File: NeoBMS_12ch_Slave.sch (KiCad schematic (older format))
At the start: 69 parts, among them IC1 LTC6804-2, P1 Low Cells, P2 High Cells, P3 BUS, P4 Expansion, Q1 Q_NPN_BCEC, SW1 Address, T1 CM Choke, T2 PE-68386N

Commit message: - integrated balancer and filter resistors into one - changed filter/balancer resistors to 1206 - changed BIAS network to 1k5 + 470R - relocated BIAS network
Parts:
- removed R10, R11, R12, R13, R2, R3, R4, R5, R6, R7, R8, R9: 100, Resistors_SMD:R_0805, symbol R
- R28, R29, R30, R31, R32, R33, R34, R35, R36, R37, R38, R39: footprint Resistors_SMD:R_0805 -> Resistors_SMD:R_1206
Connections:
- net Cell_1+: now also IC1.25 (S1)
- net Cell_10+: now also IC1.7 (S10)
- net Cell_11+: now also IC1.5 (S11)
- net Cell_12+: now also IC1.3 (S12)
- net Cell_2+: now also IC1.23 (S2)
- net Cell_3+: now also IC1.21 (S3)
- net Cell_4+: now also IC1.19 (S4)
- net Cell_5+: now also IC1.17 (S5)
- net Cell_6+: now also IC1.15 (S6)
- net Cell_7+: now also IC1.13 (S7)
- net Cell_8+: now also IC1.11 (S8)
- net Cell_9+: now also IC1.9 (S9)
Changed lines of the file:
@@
-$EndComp
-$Comp
-L R R2
-U 1 1 565ED732
-P 3250 2750
-F 0 "R2" V 3330 2750 50  0000 C CNN
-F 1 "100" V 3250 2750 50  0000 C CNN
-F 2 "Resistors_SMD:R_0805" V 3180 2750 30  0001 C CNN
-F 3 "" H 3250 2750 30  0000 C CNN
-	1    3250 2750
-	0    -1   -1   0
-$EndComp
-$Comp
-L R R3
-U 1 1 565ED81C
-P 3250 2950
-F 0 "R3" V 3330 2950 50  0000 C CNN
-F 1 "100" V 3250 2950 50  0000 C CNN
-F 2 "Resistors_SMD:R_0805" V 3180 2950 30  0001 C CNN
-F 3 "" H 3250 2950 30  0000 C CNN
-	1    3250 2950
-	0    -1   -1   0
-$EndComp
-$Comp
-L R R4
-U 1 1 565ED83F
-P 3250 3150
-F 0 "R4" V 3330 3150 50  0000 C CNN
-F 1 "100" V 3250 3150 50  0000 C CNN
-F 2 "Resistors_SMD:R_0805" V 3180 3150 30  0001 C CNN
-F 3 "" H 3250 3150 30  0000 C CNN
-	1    3250 3150
-	0    -1   -1   0
-$EndComp
-$Comp
-L R R5
-U 1 1 565ED85F
-P 3250 3350
-F 0 "R5" V 3330 3350 50  0000 C CNN
-F 1 "100" V 3250 3350 50  0000 C CNN
-F 2 "Resistors_SMD:R_0805" V 3180 3350 30  0001 C CNN
-F 3 "" H 3250 3350 30  0000 C CNN
-	1    3250 3350
-	0    -1   -1   0
-$EndComp
-$Comp
-L R R6
-U 1 1 565ED90E
-P 3250 3550
-F 0 "R6" V 3330 3550 50  0000 C CNN
-F 1 "100" V 3250 3550 50  0000 C CNN
-F 2 "Resistors_SMD:R_0805" V 3180 3550 30  0001 C CNN
-F 3 "" H 3250 3550 30  0000 C CNN
-	1    3250 3550
-	0    -1   -1   0
-$EndComp
-$Comp
-L R R7
-U 1 1 565ED934
-P 3250 3750
-F 0 "R7" V 3330 3750 50  0000 C CNN
-F 1 "100" V 3250 3750 50  0000 C CNN
-F 2 "Resistors_SMD:R_0805" V 3180 3750 30  0001 C CNN
-F 3 "" H 3250 3750 30  0000 C CNN
-	1    3250 3750
-	0    -1   -1   0
-$EndComp
-$Comp
-L R R8
-U 1 1 565ED95D
-P 3250 3950
-F 0 "R8" V 3330 3950 50  0000 C CNN
-F 1 "100" V 3250 3950 50  0000 C CNN
-F 2 "Resistors_SMD:R_0805" V 3180 3950 30  0001 C CNN
-F 3 "" H 3250 3950 30  0000 C CNN
-	1    3250 3950
-	0    -1   -1   0
-$EndComp
-$Comp
-L R R9
-U 1 1 565EDA21
-P 3250 4150
-F 0 "R9" V 3330 4150 50  0000 C CNN
-F 1 "100" V 3250 4150 50  0000 C CNN
-F 2 "Resistors_SMD:R_0805" V 3180 4150 30  0001 C CNN
-F 3 "" H 3250 4150 30  0000 C CNN
-	1    3250 4150
-	0    -1   -1   0
-$EndComp
-$Comp
-L R R10
-U 1 1 565EDA54
-P 3250 4350
-F 0 "R10" V 3330 4350 50  0000 C CNN
-F 1 "100" V 3250 4350 50  0000 C CNN
-F 2 "Resistors_SMD:R_0805" V 3180 4350 30  0001 C CNN
-F 3 "" H 3250 4350 30  0000 C CNN
-	1    3250 4350
-	0    -1   -1   0
-$EndComp
-$Comp
-L R R11
-U 1 1 565EDA86
-P 3250 4550
-F 0 "R11" V 3330 4550 50  0000 C CNN
-F 1 "100" V 3250 4550 50  0000 C CNN
-F 2 "Resistors_SMD:R_0805" V 3180 4550 30  0001 C CNN
-F 3 "" H 3250 4550 30  0000 C CNN
-	1    3250 4550
-	0    -1   -1   0
-$EndComp
-$Comp
-L R R12
-U 1 1 565EDABB
-P 3250 4750
-F 0 "R12" V 3330 4750 50  0000 C CNN
-F 1 "100" V 3250 4750 50  0000 C CNN
-F 2 "Resistors_SMD:R_0805" V 3180 4750 30  0001 C CNN
-F 3 "" H 3250 4750 30  0000 C CNN
-	1    3250 4750
-	0    -1   -1   0
-$EndComp
-$Comp
-L R R13
-U 1 1 565EDAF3
-P 5650 4850
-F 0 "R13" V 5730 4850 50  0000 C CNN
-F 1 "100" V 5650 4850 50  0000 C CNN
-F 2 "Resistors_SMD:R_0805" V 5580 4850 30  0001 C CNN
-F 3 "" H 5650 4850 30  0000 C CNN
-	1    5650 4850
-	0    -1   -1   0
 $EndComp
 $Comp
@@
 	6100 2950 6100 3050
 Wire Wire Line
-	5800 5150 5800 4850
-Wire Wire Line
-	3100 5150 5800 5150
+	5800 4850 5800 5150
+Wire Wire Line
+	5800 5150 3100 5150
 Wire Wire Line
 	3100 4750 3100 4650
@@
 	3100 3050 3100 3150
 Wire Wire Line
-	3400 2950 3850 2950
-Wire Wire Line
-	3400 3150 3850 3150
-Wire Wire Line
-	3850 3350 3400 3350
-Wire Wire Line
-	3400 3550 3850 3550
-Wire Wire Line
-	3850 3750 3400 3750
-Wire Wire Line
-	3400 3950 3850 3950
-Wire Wire Line
-	3850 4150 3400 4150
-Wire Wire Line
-	3850 4350 3400 4350
-Wire Wire Line
-	3400 4550 3850 4550
-Wire Wire Line
-	3850 4750 3400 4750
-Wire Wire Line
-	5500 4850 5350 4850
-Wire Wire Line
-	3850 2750 3400 2750
+	3100 2950 3850 2950
+Wire Wire Line
+	3100 3150 3850 3150
+Wire Wire Line
+	3100 3350 3850 3350
+Wire Wire Line
+	3100 3550 3850 3550
+Wire Wire Line
+	3100 3750 3850 3750
+Wire Wire Line
+	3100 3950 3850 3950
+Wire Wire Line
+	3100 4150 3850 4150
+Wire Wire Line
+	3100 4350 3850 4350
+Wire Wire Line
+	3100 4550 3850 4550
+Wire Wire Line
+	3100 4750 3850 4750
+Wire Wire Line
+	5350 4850 5800 4850
+Wire Wire Line
+	3100 2750 3850 2750
 Wire Wire Line
 	6800 2900 6800 3350
@@
 F 0 "R28" V 3330 2650 50  0000 C CNN
 F 1 "100" V 3250 2650 50  0000 C CNN
-F 2 "Resistors_SMD:R_0805" V 3180 2650 30  0001 C CNN
+F 2 "Resistors_SMD:R_1206" V 3180 2650 30  0001 C CNN
 F 3 "" H 3250 2650 30  0000 C CNN
 	1    3250 2650
@@
 F 0 "R29" V 3330 2850 50  0000 C CNN
 F 1 "100" V 3250 2850 50  0000 C CNN
-F 2 "Resistors_SMD:R_0805" V 3180 2850 30  0001 C CNN
+F 2 "Resistors_SMD:R_1206" V 3180 2850 30  0001 C CNN
 F 3 "" H 3250 2850 30  0000 C CNN
 	1    3250 2850
@@
 F 0 "R30" V 3330 3050 50  0000 C CNN
 F 1 "100" V 3250 3050 50  0000 C CNN
-F 2 "Resistors_SMD:R_0805" V 3180 3050 30  0001 C CNN
+F 2 "Resistors_SMD:R_1206" V 3180 3050 30  0001 C CNN
 F 3 "" H 3250 3050 30  0000 C CNN
 	1    3250 3050
@@
 F 0 "R31" V 3330 3250 50  0000 C CNN
 F 1 "100" V 3250 3250 50  0000 C CNN
-F 2 "Resistors_SMD:R_0805" V 3180 3250 30  0001 C CNN
+F 2 "Resistors_SMD:R_1206" V 3180 3250 30  0001 C CNN
 F 3 "" H 3250 3250 30  0000 C CNN
 	1    3250 3250
@@
 F 0 "R32" V 3330 3450 50  0000 C CNN
 F 1 "100" V 3250 3450 50  0000 C CNN
-F 2 "Resistors_SMD:R_0805" V 3180 3450 30  0001 C CNN
+F 2 "Resistors_SMD:R_1206" V 3180 3450 30  0001 C CNN
 F 3 "" H 3250 3450 30  0000 C CNN
 	1    3250 3450
@@
 F 0 "R33" V 3330 3650 50  0000 C CNN
 F 1 "100" V 3250 3650 50  0000 C CNN
-F 2 "Resistors_SMD:R_0805" V 3180 3650 30  0001 C CNN
+F 2 "Resistors_SMD:R_1206" V 3180 3650 30  0001 C CNN
 F 3 "" H 3250 3650 30  0000 C CNN
 	1    3250 3650
@@
 F 0 "R34" V 3330 3850 50  0000 C CNN
 F 1 "100" V 3250 3850 50  0000 C CNN
-F 2 "Resistors_SMD:R_0805" V 3180 3850 30  0001 C CNN
+F 2 "Resistors_SMD:R_1206" V 3180 3850 30  0001 C CNN
 F 3 "" H 3250 3850 30  0000 C CNN
 	1    3250 3850
@@
 F 0 "R35" V 3330 4050 50  0000 C CNN
 F 1 "100" V 3250 4050 50  0000 C CNN
-F 2 "Resistors_SMD:R_0805" V 3180 4050 30  0001 C CNN
+F 2 "Resistors_SMD:R_1206" V 3180 4050 30  0001 C CNN
 F 3 "" H 3250 4050 30  0000 C CNN
 	1    3250 4050
@@
 F 0 "R36" V 3330 4250 50  0000 C CNN
 F 1 "100" V 3250 4250 50  0000 C CNN
-F 2 "Resistors_SMD:R_0805" V 3180 4250 30  0001 C CNN
+F 2 "Resistors_SMD:R_1206" V 3180 4250 30  0001 C CNN
 F 3 "" H 3250 4250 30  0000 C CNN
 	1    3250 4250
@@
 F 0 "R37" V 3330 4450 50  0000 C CNN
 F 1 "100" V 3250 4450 50  0000 C CNN
-F 2 "Resistors_SMD:R_0805" V 3180 4450 30  0001 C CNN
+F 2 "Resistors_SMD:R_1206" V 3180 4450 30  0001 C CNN
 F 3 "" H 3250 4450 30  0000 C CNN
 	1    3250 4450
@@
 F 0 "R38" V 3330 4650 50  0000 C CNN
 F 1 "100" V 3250 4650 50  0000 C CNN
-F 2 "Resistors_SMD:R_0805" V 3180 4650 30  0001 C CNN
+F 2 "Resistors_SMD:R_1206" V 3180 4650 30  0001 C CNN
 F 3 "" H 3250 4650 30  0000 C CNN
 	1    3250 4650
@@
 F 0 "R39" V 3330 4850 50  0000 C CNN
 F 1 "100" V 3250 4850 50  0000 C CNN
-F 2 "Resistors_SMD:R_0805" V 3180 4850 30  0001 C CNN
+F 2 "Resistors_SMD:R_1206" V 3180 4850 30  0001 C CNN
 F 3 "" H 3250 4850 30  0000 C CNN
 	1    3250 4850

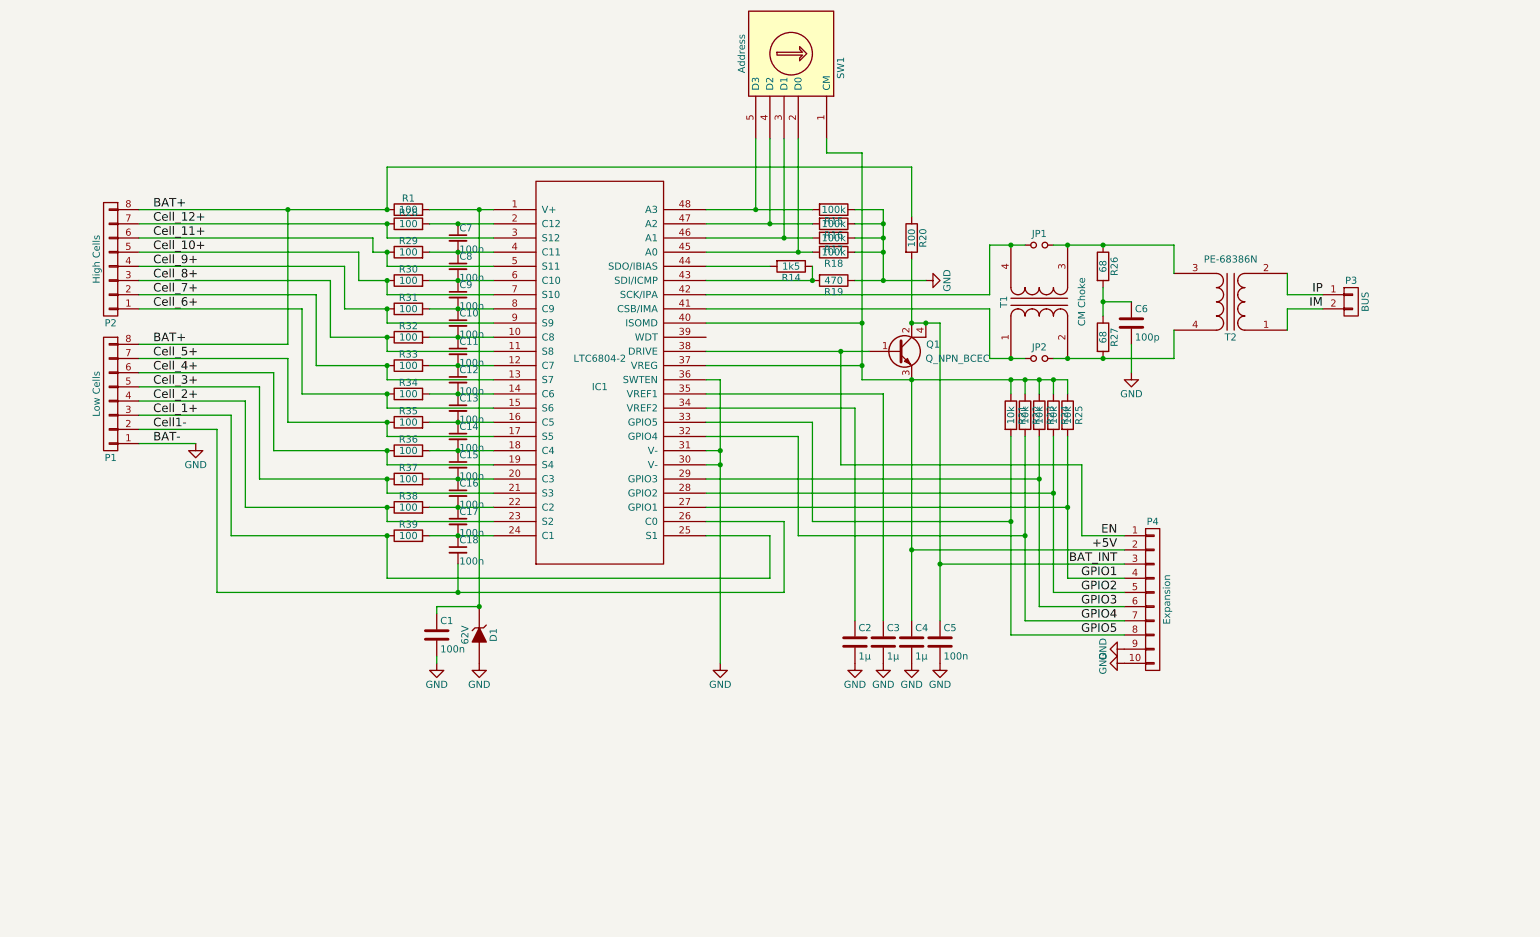
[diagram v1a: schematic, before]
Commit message: - jump to version 2.0 - external balancing switches
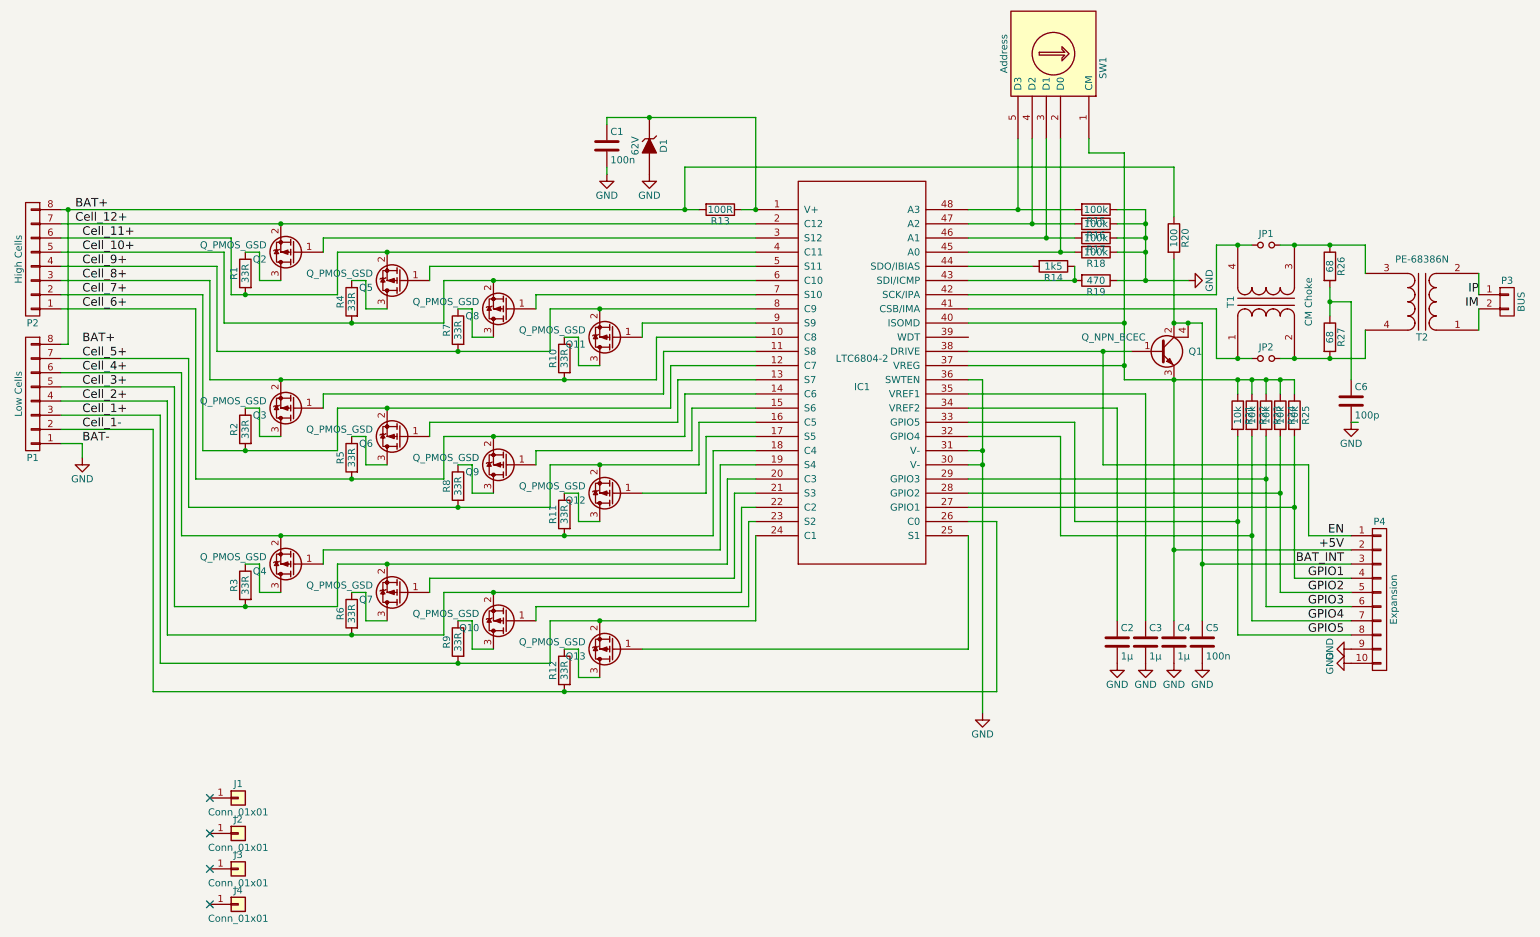
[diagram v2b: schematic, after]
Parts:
- removed C10, C11, C12, C13, C14, C15, C16, C17, C18, C7, C8, C9: 100n, Capacitors_SMD:C_0805, symbol C_Small
- removed R28, R29, R30, R31, R32, R33, R34, R35, R36, R37, R38, R39: 100, Resistors_SMD:R_1206, symbol R
- added J1, J2, J3, J4: Conn_01x01, Mounting_Holes:MountingHole_3.5mm, symbol Conn_01x01
- added Q10, Q11, Q12, Q13, Q2, Q3, Q4, Q5, Q6, Q7, Q8, Q9: Q_PMOS_GSD, TO_SOT_Packages_SMD:SOT-23, symbol Q_PMOS_GSD
- added R10, R11, R12, R2, R3, R4, R5, R6, R7, R8, R9: 33R, Resistors_SMD:R_1210, symbol R
- added R13: 100R, Resistors_SMD:R_0805, symbol R
- JP1, JP2: footprint Resistors_SMD:R_0603 -> alexmod:Jumper_2
- R1: value 100 -> 33R; footprint Resistors_SMD:R_0805 -> Resistors_SMD:R_1210
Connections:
- net BAT+: now also R13.2; no longer R1.1
- net Cell_1+: now also IC1.24 (C1), Q13.2 (S), R9.2; no longer IC1.25 (S1)
- net Cell_10+: now also IC1.6 (C10), Q8.2 (S), R4.2; no longer IC1.7 (S10)
- net Cell_11+: now also IC1.4 (C11), R1.2, Q5.2 (S); no longer IC1.5 (S11)
- net Cell_12+: now also IC1.2 (C12), Q2.2 (S); no longer IC1.3 (S12)
- net Cell_2+: now also IC1.22 (C2), Q10.2 (S), R6.2; no longer IC1.23 (S2)
- net Cell_3+: now also IC1.20 (C3), Q7.2 (S), R3.2; no longer IC1.21 (S3)
- net Cell_4+: now also IC1.18 (C4), Q4.2 (S), R11.2; no longer IC1.19 (S4)
- net Cell_5+: now also IC1.16 (C5), Q12.2 (S), R8.2; no longer IC1.17 (S5)
- net Cell_6+: now also IC1.14 (C6), Q9.2 (S), R5.2; no longer IC1.15 (S6)
- net Cell_7+: now also IC1.12 (C7), Q6.2 (S), R2.2; no longer IC1.13 (S7)
- net Cell_8+: now also IC1.10 (C8), Q3.2 (S), R10.2; no longer IC1.11 (S8)
- net Cell_9+: now also IC1.8 (C9), Q11.2 (S), R7.2; no longer IC1.9 (S9)
- net at C1.1, D1.1 (K), IC1.1 (V+): now also R13.1; no longer R1.2
- net Cell1- renamed Cell_1-
- net Cell_1-: now also R12.2
- new net: IC1.11 (S8), Q3.1 (G)
- new net: IC1.13 (S7), Q6.1 (G)
- new net: IC1.15 (S6), Q9.1 (G)
- new net: IC1.17 (S5), Q12.1 (G)
- new net: IC1.19 (S4), Q4.1 (G)
- new net: IC1.21 (S3), Q7.1 (G)
- new net: IC1.23 (S2), Q10.1 (G)
- new net: IC1.25 (S1), Q13.1 (G)
- new net: IC1.3 (S12), Q2.1 (G)
- new net: IC1.5 (S11), Q5.1 (G)
- new net: IC1.7 (S10), Q8.1 (G)
- new net: IC1.9 (S9), Q11.1 (G)
- new net: Q2.3 (D), R1.1
- new net: Q5.3 (D), R4.1
- new net: Q8.3 (D), R7.1
- new net: Q11.3 (D), R10.1
- new net: Q3.3 (D), R2.1
- new net: Q6.3 (D), R5.1
- new net: Q9.3 (D), R8.1
- new net: Q12.3 (D), R11.1
- new net: Q4.3 (D), R3.1
- new net: Q7.3 (D), R6.1
- new net: Q10.3 (D), R9.1
- new net: Q13.3 (D), R12.1
- no-connect marks 0 -> 4
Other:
- moved on the sheet: C1, C2, C3, C4, C5, C6, D1, IC1, JP1, JP2, P1, P2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
